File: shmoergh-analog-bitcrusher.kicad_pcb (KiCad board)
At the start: 2 copper layers, 35 x 60 mm, 36 parts, among them J2 Eurorack power, Q1 2N3819, U1 TL074, U2 TL072

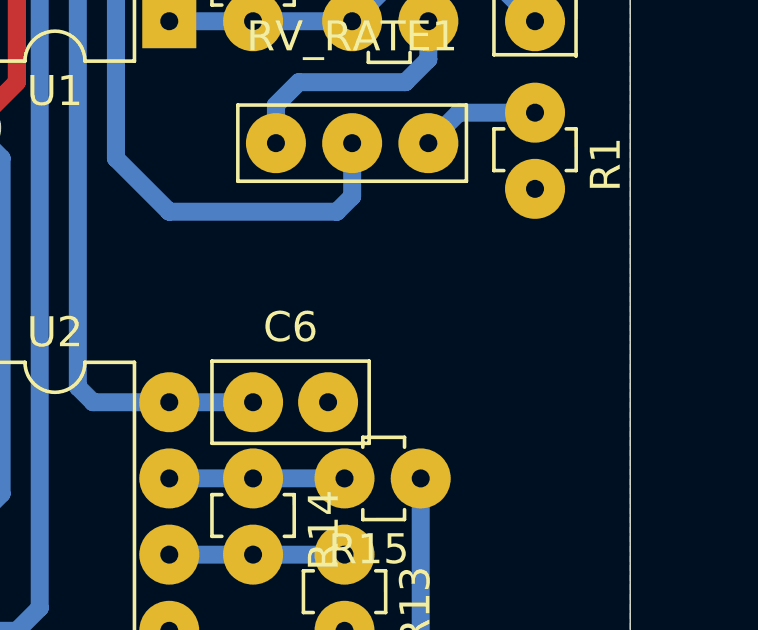
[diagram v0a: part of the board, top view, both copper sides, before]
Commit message: Added on/off switch to schematics
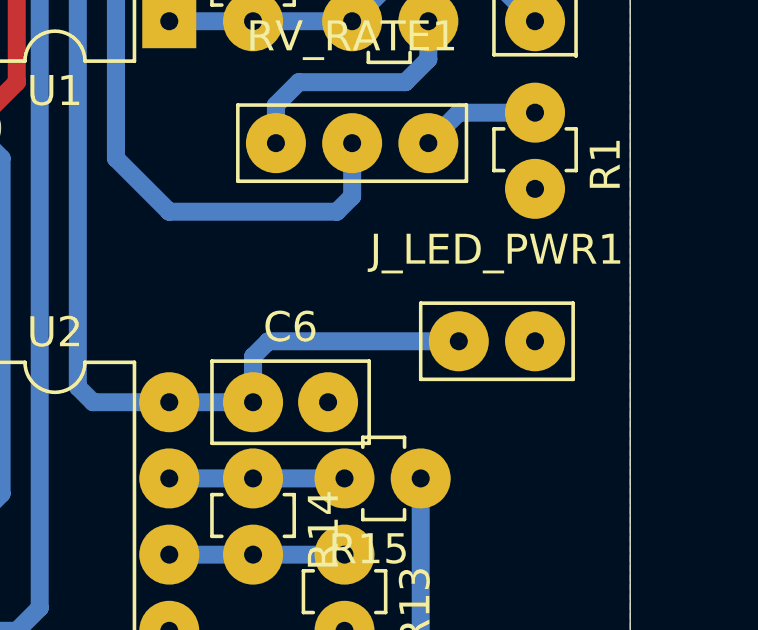
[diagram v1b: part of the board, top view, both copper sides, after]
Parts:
- added J_LED_PWR1: LED Power, Zimo_Manual_PCB:NSL25_01x02_Vertical, F.Cu at (131.8, 92.5)
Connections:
- net /AUDIO_IN renamed RAW_INPUT
- net Net-(J_AUDIO_OUT1-PadT) renamed FX_OUT
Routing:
- net +12V: track 78.0 -> 86.6 mm
